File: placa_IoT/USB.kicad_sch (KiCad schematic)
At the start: 9 parts, among them J4 USB4105-GF-A-120

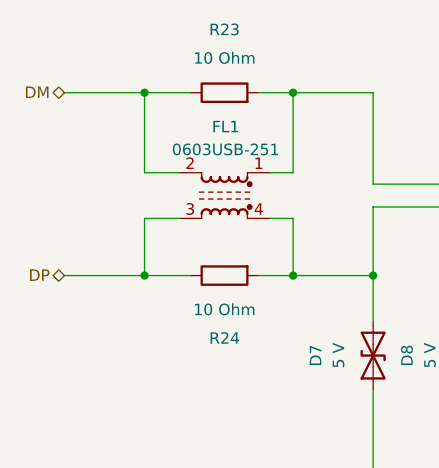
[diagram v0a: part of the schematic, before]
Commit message: Falta unir pines
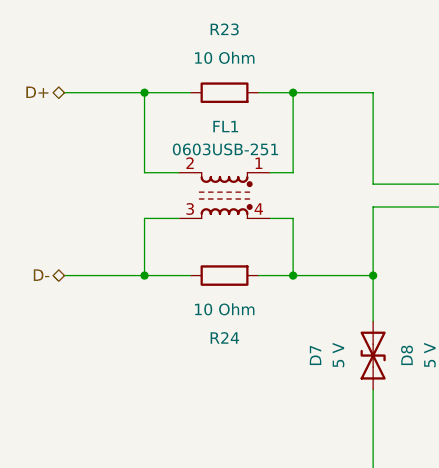
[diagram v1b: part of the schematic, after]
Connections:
- net DM renamed D+
- net DP renamed D-
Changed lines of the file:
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@@
 		)
 	)
-	(hierarchical_label "DM"
+	(hierarchical_label "D-"
 		(shape bidirectional)
-		(at 63.5 60.96 180)
+		(at 63.5 81.28 180)
 		(effects
 			(font
@@
 		)
 	)
-	(hierarchical_label "DP"
+	(hierarchical_label "D+"
 		(shape bidirectional)
-		(at 63.5 81.28 180)
+		(at 63.5 60.96 180)
 		(effects
 			(font
